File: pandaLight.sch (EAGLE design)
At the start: 163 parts, among them J1 PJ-037A, U1 MIC23450AAAYML, U10 51, U11 TPD12S016PWR, U12 N25Q128AF8, U13 TPD12S016PWR, U14 AS4C128M16D3, U15 PMOD-2X6, U16 PMOD-2X6, U17 PLR135-T10, U18 PLT133-T10W, U19 PLR135-T10, U2 6SLX45CSG324, U20 TP10SQ, U21 TP10SQ, U22 PAN1322, U3 TPD4S014SON, U4 FT2232HL, U5 93LC46BT-I/OT, U6 51, U7 51, U8 TPD12S016PWR, U9 51, X1 USBUB-S, X2 HDMI_RECEPTICAL_A, X3 HDMI_RECEPTICAL_A, X4 HDMI_RECEPTICAL_A, Y1 403, Y2 20Mhz

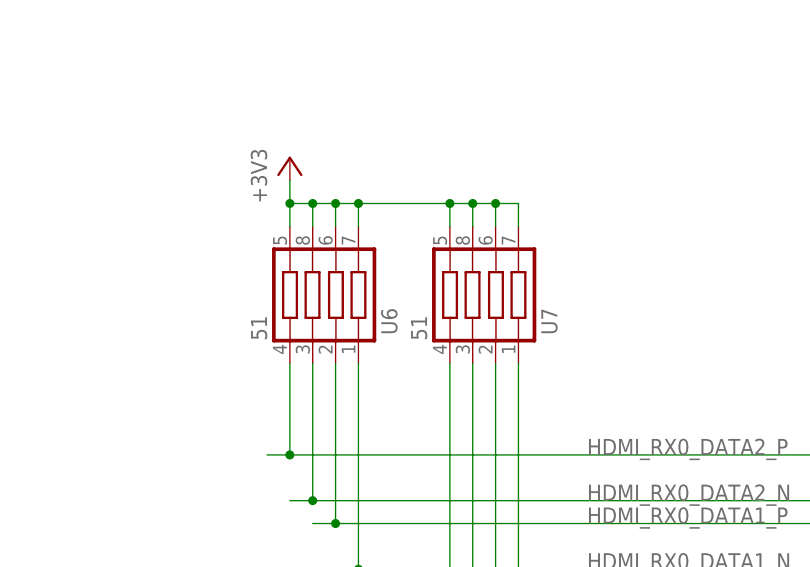
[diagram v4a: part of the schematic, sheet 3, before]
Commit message: Moved the pullup resistor networks and removed vias from the HDMI_RX* traces
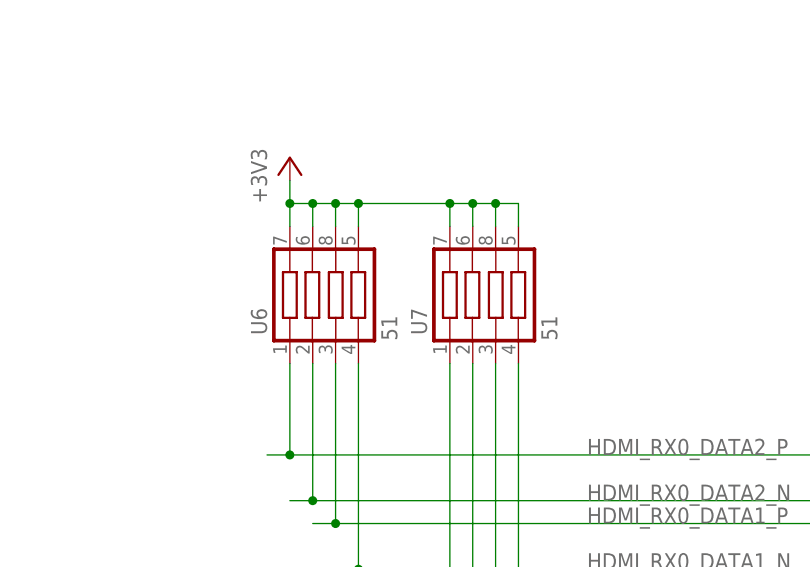
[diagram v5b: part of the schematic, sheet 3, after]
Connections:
- net HDMI_RX0_CLK_N: now also U7.4; no longer U7.1
- net HDMI_RX0_CLK_P: now also U7.3; no longer U7.2
- net HDMI_RX0_DATA0_N: now also U7.2; no longer U7.3
- net HDMI_RX0_DATA0_P: now also U7.1; no longer U7.4
- net HDMI_RX0_DATA1_N: now also U6.4; no longer U6.1
- net HDMI_RX0_DATA1_P: now also U6.3; no longer U6.2
- net HDMI_RX0_DATA2_N: now also U6.2; no longer U6.3
- net HDMI_RX0_DATA2_P: now also U6.1; no longer U6.4
- net HDMI_RX1_CLK_N: now also U10.4; no longer U10.1
- net HDMI_RX1_CLK_P: now also U10.3; no longer U10.2
- net HDMI_RX1_DATA0_N: now also U10.2; no longer U10.3
- net HDMI_RX1_DATA0_P: now also U10.1; no longer U10.4
- net HDMI_RX1_DATA1_N: now also U9.4; no longer U9.1
- net HDMI_RX1_DATA1_P: now also U9.3; no longer U9.2
- net HDMI_RX1_DATA2_N: now also U9.2; no longer U9.3
- net HDMI_RX1_DATA2_P: now also U9.1; no longer U9.4

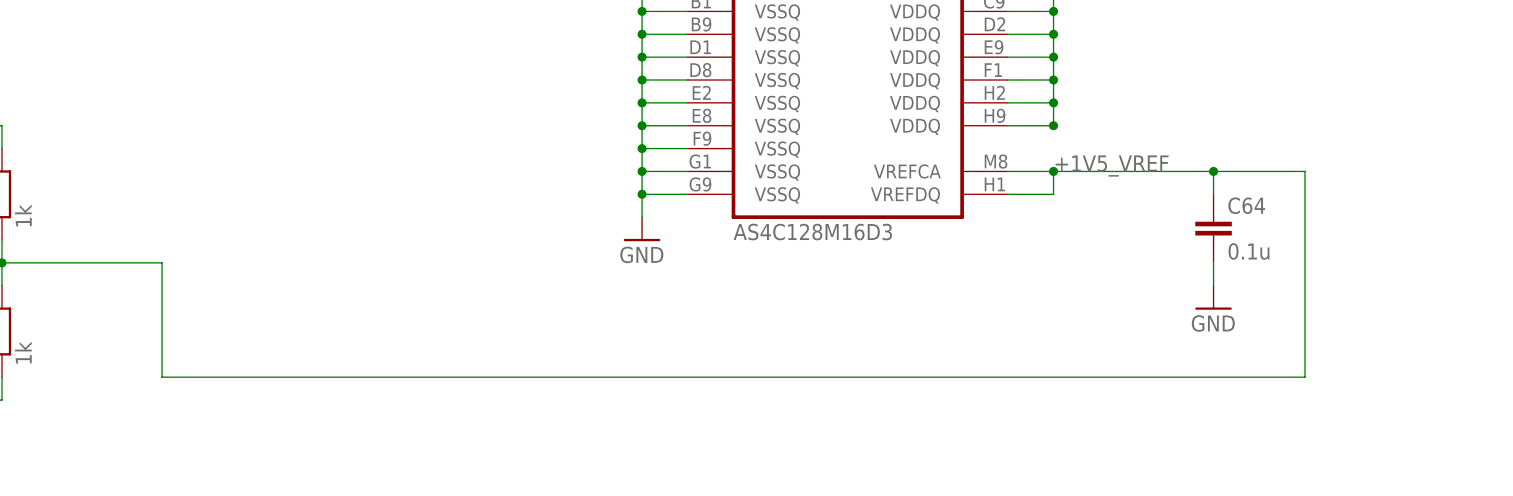
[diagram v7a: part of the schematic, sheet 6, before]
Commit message: Some tweaking and length matching of the DDR3 traces
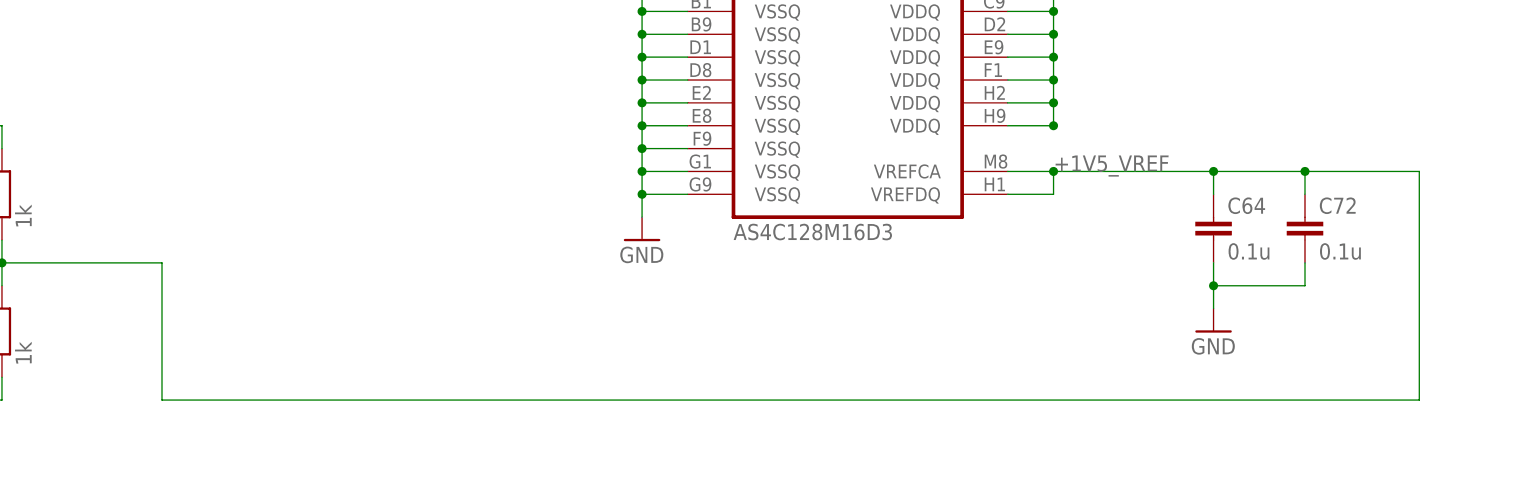
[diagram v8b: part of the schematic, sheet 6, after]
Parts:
- added C72: 0.1u, pandaLight:CAPACITOR0402
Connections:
- net +1V5_VREF: now also C72.1
- net GND: now also C72.2
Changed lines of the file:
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@@
 <attribute name="PARTNO" value="741C083510JP"/>
 </part>
+<part name="C72" library="pandaLight" deviceset="CAPACITOR" device="0402" value="0.1u">
+<attribute name="PARTNO" value="CL05B104KP5NNNC"/>
+</part>
 </parts>
 <sheets>
@@
 <attribute name="PARTNO" x="254" y="30.48" size="1.778" layer="96" display="off"/>
 </instance>
-<instance part="GND52" gate="1" x="254" y="20.32"/>
+<instance part="GND52" gate="1" x="254" y="17.78"/>
 <instance part="C65" gate="G$1" x="66.04" y="20.32">
 <attribute name="PARTNO" x="66.04" y="20.32" size="1.778" layer="96" display="off"/>
@@
 <instance part="GND50" gate="1" x="246.38" y="66.04"/>
 <instance part="GND46" gate="1" x="20.32" y="185.42"/>
+<instance part="C72" gate="G$1" x="264.16" y="30.48">
+<attribute name="PARTNO" x="264.16" y="30.48" size="1.778" layer="96" display="off"/>
+</instance>
 </instances>
 <busses>
@@
 <pinref part="GND52" gate="1" pin="GND"/>
 <wire x1="254" y1="25.4" x2="254" y2="22.86" width="0.1524" layer="91"/>
+<pinref part="C72" gate="G$1" pin="2"/>
+<wire x1="254" y1="22.86" x2="254" y2="20.32" width="0.1524" layer="91"/>
+<wire x1="254" y1="22.86" x2="264.16" y2="22.86" width="0.1524" layer="91"/>
+<wire x1="264.16" y1="22.86" x2="264.16" y2="25.4" width="0.1524" layer="91"/>
+<junction x="254" y="22.86"/>
 </segment>
 <segment>
@@
 <wire x1="254" y1="33.02" x2="254" y2="35.56" width="0.1524" layer="91"/>
 <wire x1="254" y1="35.56" x2="264.16" y2="35.56" width="0.1524" layer="91"/>
-<wire x1="264.16" y1="35.56" x2="264.16" y2="12.7" width="0.1524" layer="91"/>
-<wire x1="264.16" y1="12.7" x2="137.16" y2="12.7" width="0.1524" layer="91"/>
-<wire x1="137.16" y1="12.7" x2="137.16" y2="25.4" width="0.1524" layer="91"/>
+<wire x1="264.16" y1="35.56" x2="276.86" y2="35.56" width="0.1524" layer="91"/>
+<wire x1="276.86" y1="35.56" x2="276.86" y2="10.16" width="0.1524" layer="91"/>
+<wire x1="276.86" y1="10.16" x2="137.16" y2="10.16" width="0.1524" layer="91"/>
+<wire x1="137.16" y1="10.16" x2="137.16" y2="25.4" width="0.1524" layer="91"/>
 <pinref part="C65" gate="G$1" pin="1"/>
 <wire x1="66.04" y1="22.86" x2="66.04" y2="25.4" width="0.1524" layer="91"/>
@@
 <junction x="66.04" y="25.4"/>
 <junction x="254" y="35.56"/>
+<pinref part="C72" gate="G$1" pin="1"/>
+<wire x1="264.16" y1="33.02" x2="264.16" y2="35.56" width="0.1524" layer="91"/>
+<junction x="264.16" y="35.56"/>
 </segment>
 <segment>
